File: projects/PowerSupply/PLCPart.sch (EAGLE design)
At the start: 15 parts, among them IC1 L7815CV, IC2 L7915CV, IC3 L7805CV, X1 IN

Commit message: fix: small fix applied
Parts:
- X2: value (none) -> VCC
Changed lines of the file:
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@@
 <part name="C9" library="rcl" library_urn="urn:adsk.eagle:library:334" deviceset="CPOL-EU" device="E2.5-6" package3d_urn="urn:adsk.eagle:package:23349/1" value="100µF"/>
 <part name="C10" library="rcl" library_urn="urn:adsk.eagle:library:334" deviceset="C-EU" device="050-024X044" package3d_urn="urn:adsk.eagle:package:23643/1" value="0.1µF"/>
-<part name="X2" library="con-wago-500" library_urn="urn:adsk.eagle:library:195" deviceset="W237-4" device="" package3d_urn="urn:adsk.eagle:package:10695/1"/>
+<part name="X2" library="con-wago-500" library_urn="urn:adsk.eagle:library:195" deviceset="W237-4" device="" package3d_urn="urn:adsk.eagle:package:10695/1" value="VCC"/>
 <part name="P+6" library="bb84-supply" deviceset="+12V" device=""/>
 <part name="P-3" library="bb84-supply" deviceset="-12V" device=""/>

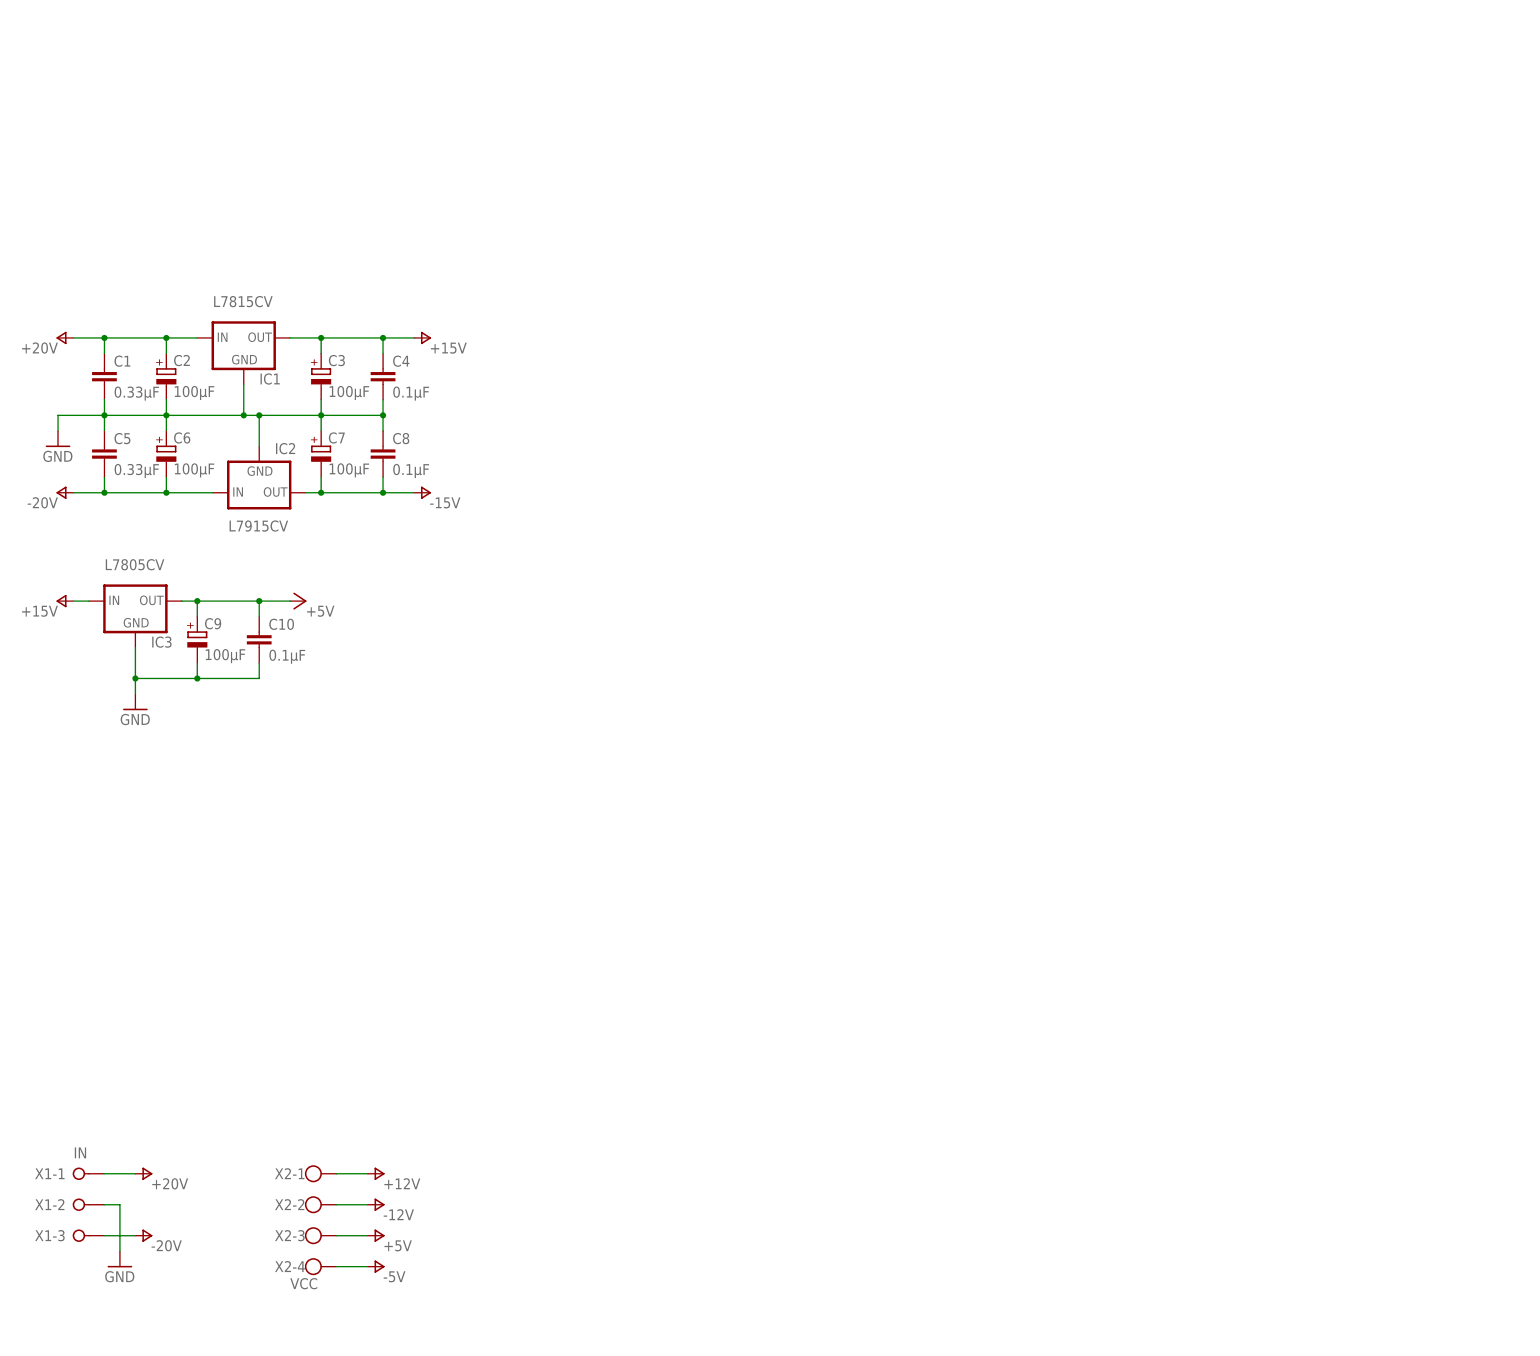
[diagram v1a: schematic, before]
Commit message: feat: amplifiers added
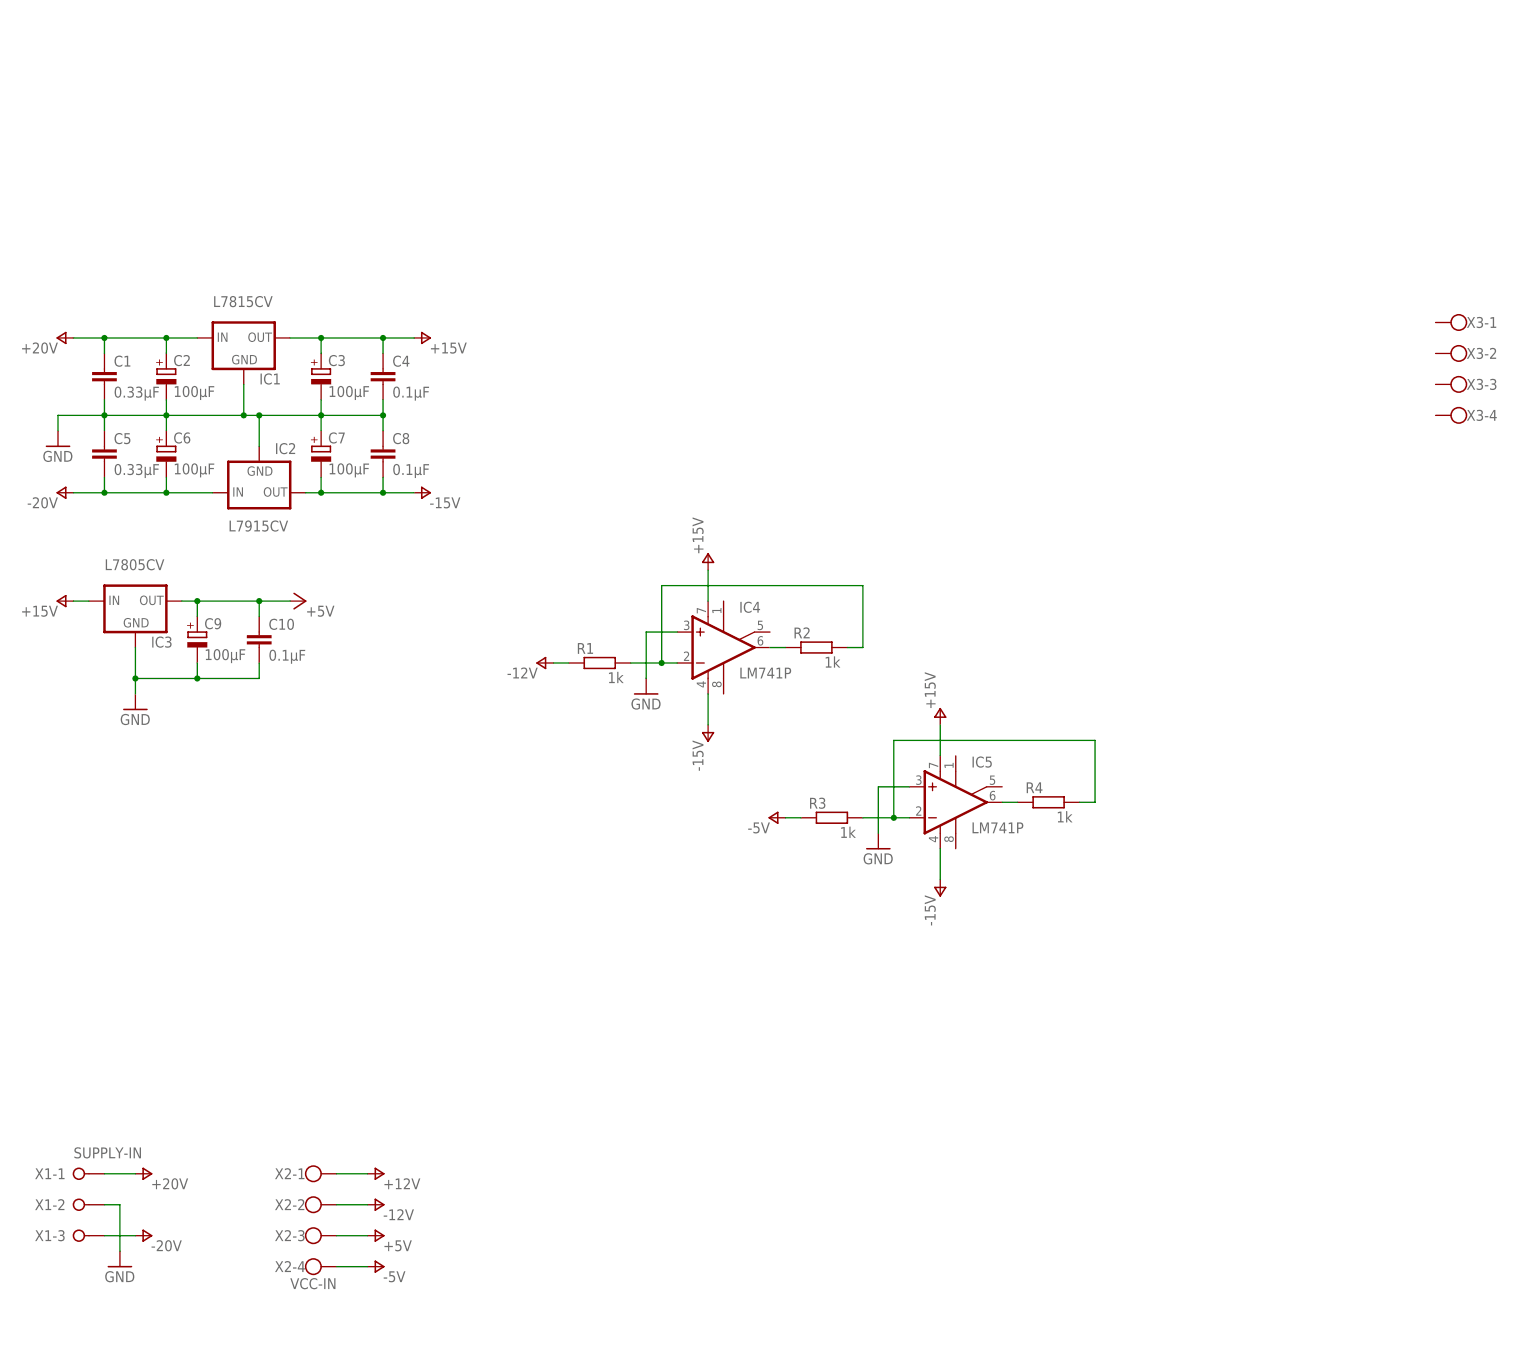
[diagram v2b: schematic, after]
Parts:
- added IC4, IC5: LM741P, linear:LM741P
- added R1, R2, R3, R4: 1k, rcl:R-EU_0207/10
- added X3: (no value), con-wago-500:W237-4
- X1: value IN -> SUPPLY-IN
- X2: value VCC -> VCC-IN
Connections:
- new net N$1: IC4.-IN, R1.2, R2.2
- new net N$2: IC5.-IN, R3.2, R4.2
- new net N$3: IC4.OUT, R2.1
- new net N$4: IC5.OUT, R4.1
- net +15V: now also IC4.V+, IC5.V+
- net -12V: now also R1.1
- net -15V: now also IC4.V-, IC5.V-
- net -5V: now also R3.1
- net GND: now also IC4.+IN, IC5.+IN

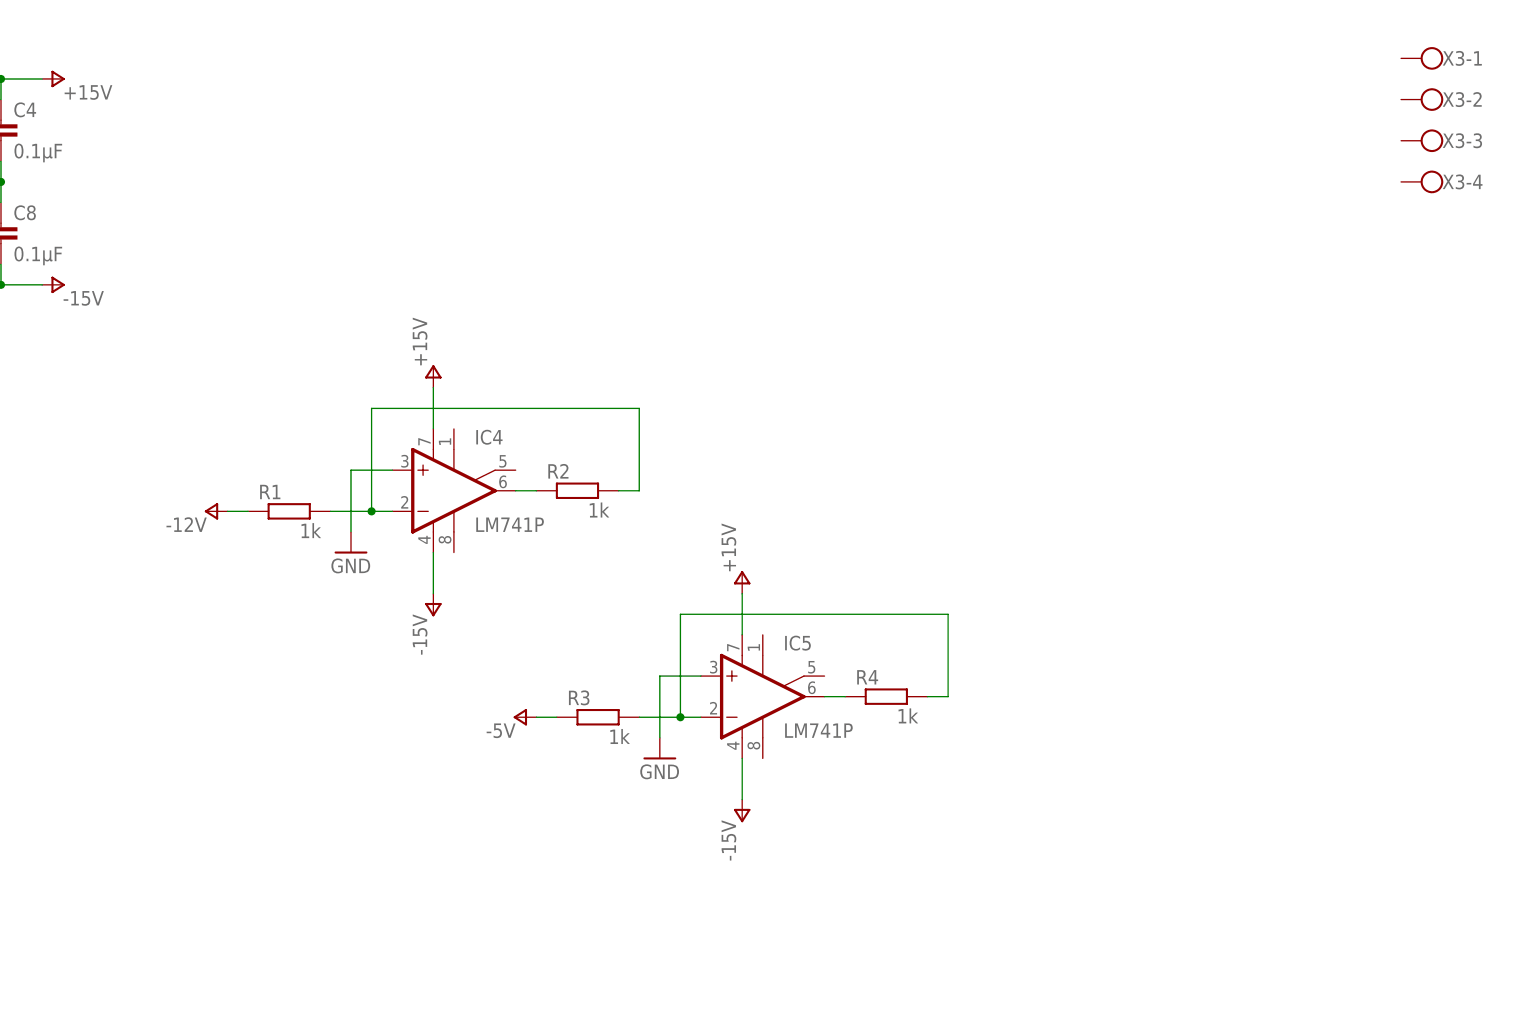
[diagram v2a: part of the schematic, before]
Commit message: feat: operation amplifiers finished
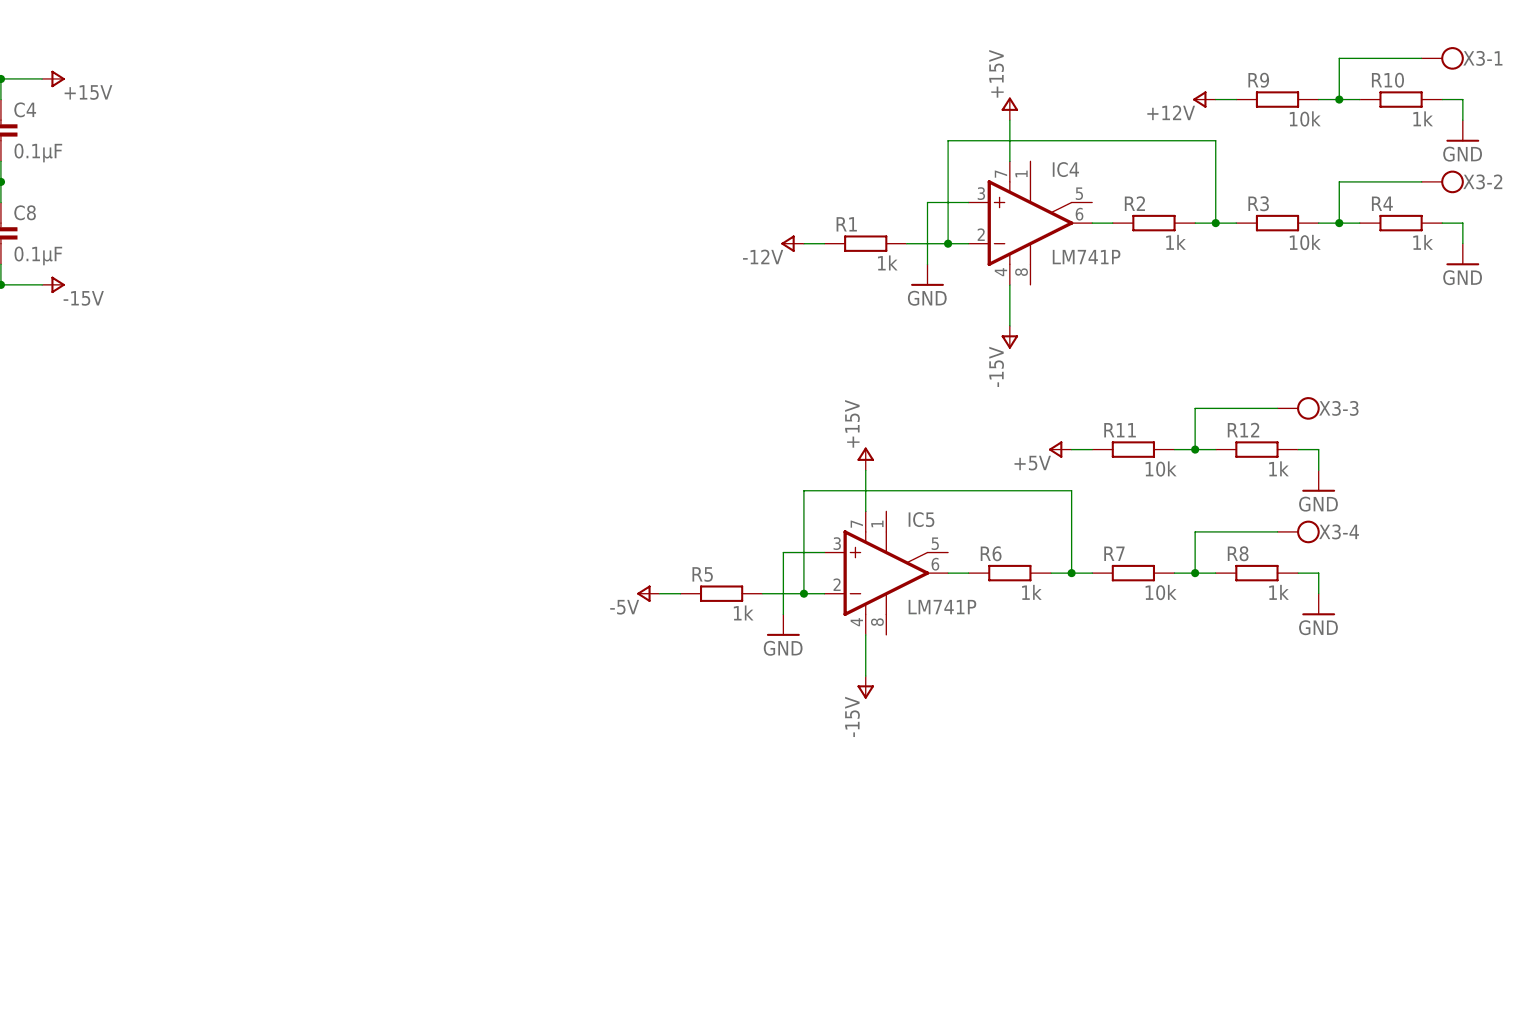
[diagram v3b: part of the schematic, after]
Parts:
- added R10, R12, R5, R6, R8: 1k, rcl:R-EU_0207/10
- added R11, R7, R9: 10k, rcl:R-EU_0207/10
- R3: value 1k -> 10k
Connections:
- new net N$10: R11.2, R12.1, X3-3.KL
- new net N$5: IC5.OUT, R6.1
- new net N$6: R7.2, R8.1, X3-4.KL
- new net N$8: R10.1, R9.2, X3-1.KL
- net +12V: now also R9.1
- net +5V: now also R11.1
- net -5V: now also R5.1; no longer R3.1
- net GND: now also R10.2, R12.2, R4.2, R8.2
- net N$1: now also R3.1
- net N$2: now also R4.1, X3-2.KL; no longer IC5.-IN, R4.2
- net N$4: now also IC5.-IN, R5.2, R6.2, R7.1; no longer IC5.OUT, R4.1
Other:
- moved on the sheet: IC4, IC5, R1, R2, R3, R4, X3-1, X3-2, X3-3, X3-4
